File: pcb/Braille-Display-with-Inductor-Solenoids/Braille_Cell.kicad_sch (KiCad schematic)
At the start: 15 parts, among them U2 TPIC6595

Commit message: Remove symbol and footprint libraries
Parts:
- L1, L2, L3, L4, L5, L6: footprint 00-project-footprint-lib:Inductor_0805_2012Metric_SMD_Vertical_Square -> 00-project-footprints:Inductor_0805_2012Metric_SMD_Vertical_Square
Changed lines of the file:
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@@
 			)
 		)
-		(property "Footprint" "00-project-footprint-lib:Inductor_0805_2012Metric_SMD_Vertical_Square"
+		(property "Footprint" "00-project-footprints:Inductor_0805_2012Metric_SMD_Vertical_Square"
 			(at 107.95 66.04 0)
 			(effects
@@
 			)
 		)
-		(property "Footprint" "00-project-footprint-lib:Inductor_0805_2012Metric_SMD_Vertical_Square"
+		(property "Footprint" "00-project-footprints:Inductor_0805_2012Metric_SMD_Vertical_Square"
 			(at 107.95 52.07 0)
 			(effects
@@
 			)
 		)
-		(property "Footprint" "00-project-footprint-lib:Inductor_0805_2012Metric_SMD_Vertical_Square"
+		(property "Footprint" "00-project-footprints:Inductor_0805_2012Metric_SMD_Vertical_Square"
 			(at 121.92 66.04 0)
 			(effects
@@
 			)
 		)
-		(property "Footprint" "00-project-footprint-lib:Inductor_0805_2012Metric_SMD_Vertical_Square"
+		(property "Footprint" "00-project-footprints:Inductor_0805_2012Metric_SMD_Vertical_Square"
 			(at 107.95 38.1 0)
 			(effects
@@
 			)
 		)
-		(property "Footprint" "00-project-footprint-lib:Inductor_0805_2012Metric_SMD_Vertical_Square"
+		(property "Footprint" "00-project-footprints:Inductor_0805_2012Metric_SMD_Vertical_Square"
 			(at 121.92 38.1 0)
 			(effects
@@
 			)
 		)
-		(property "Footprint" "00-project-footprint-lib:Inductor_0805_2012Metric_SMD_Vertical_Square"
+		(property "Footprint" "00-project-footprints:Inductor_0805_2012Metric_SMD_Vertical_Square"
 			(at 121.92 52.07 0)
 			(effects

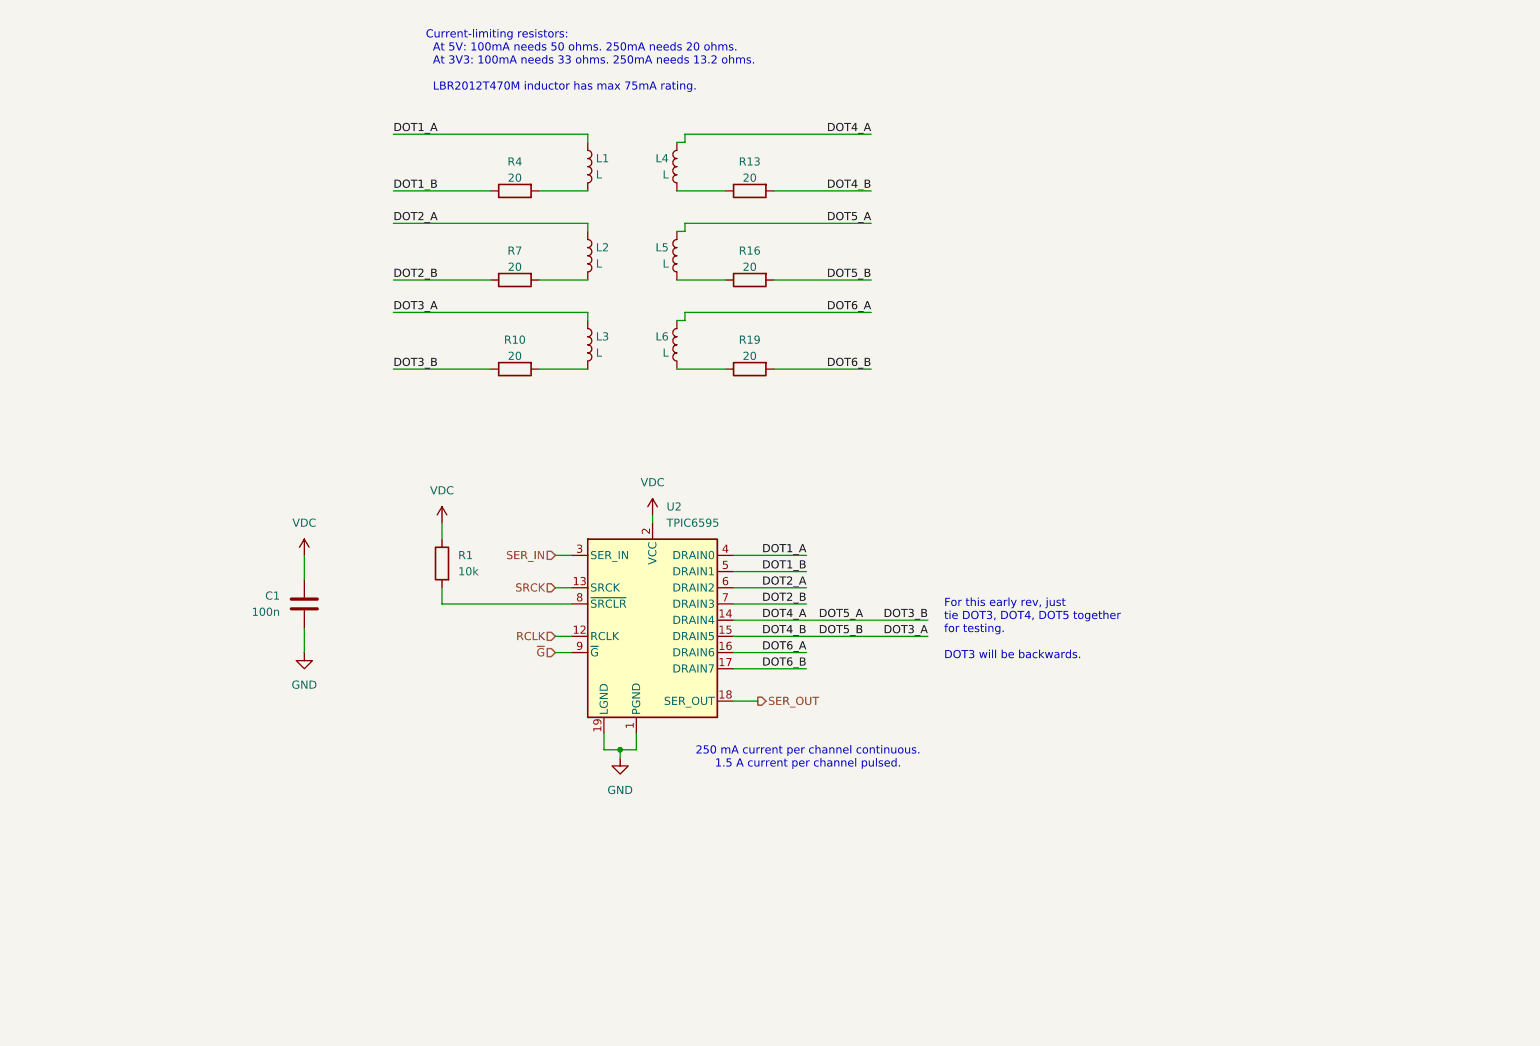
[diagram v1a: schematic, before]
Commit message: Add both inductors on same PCB, switch to new drivers
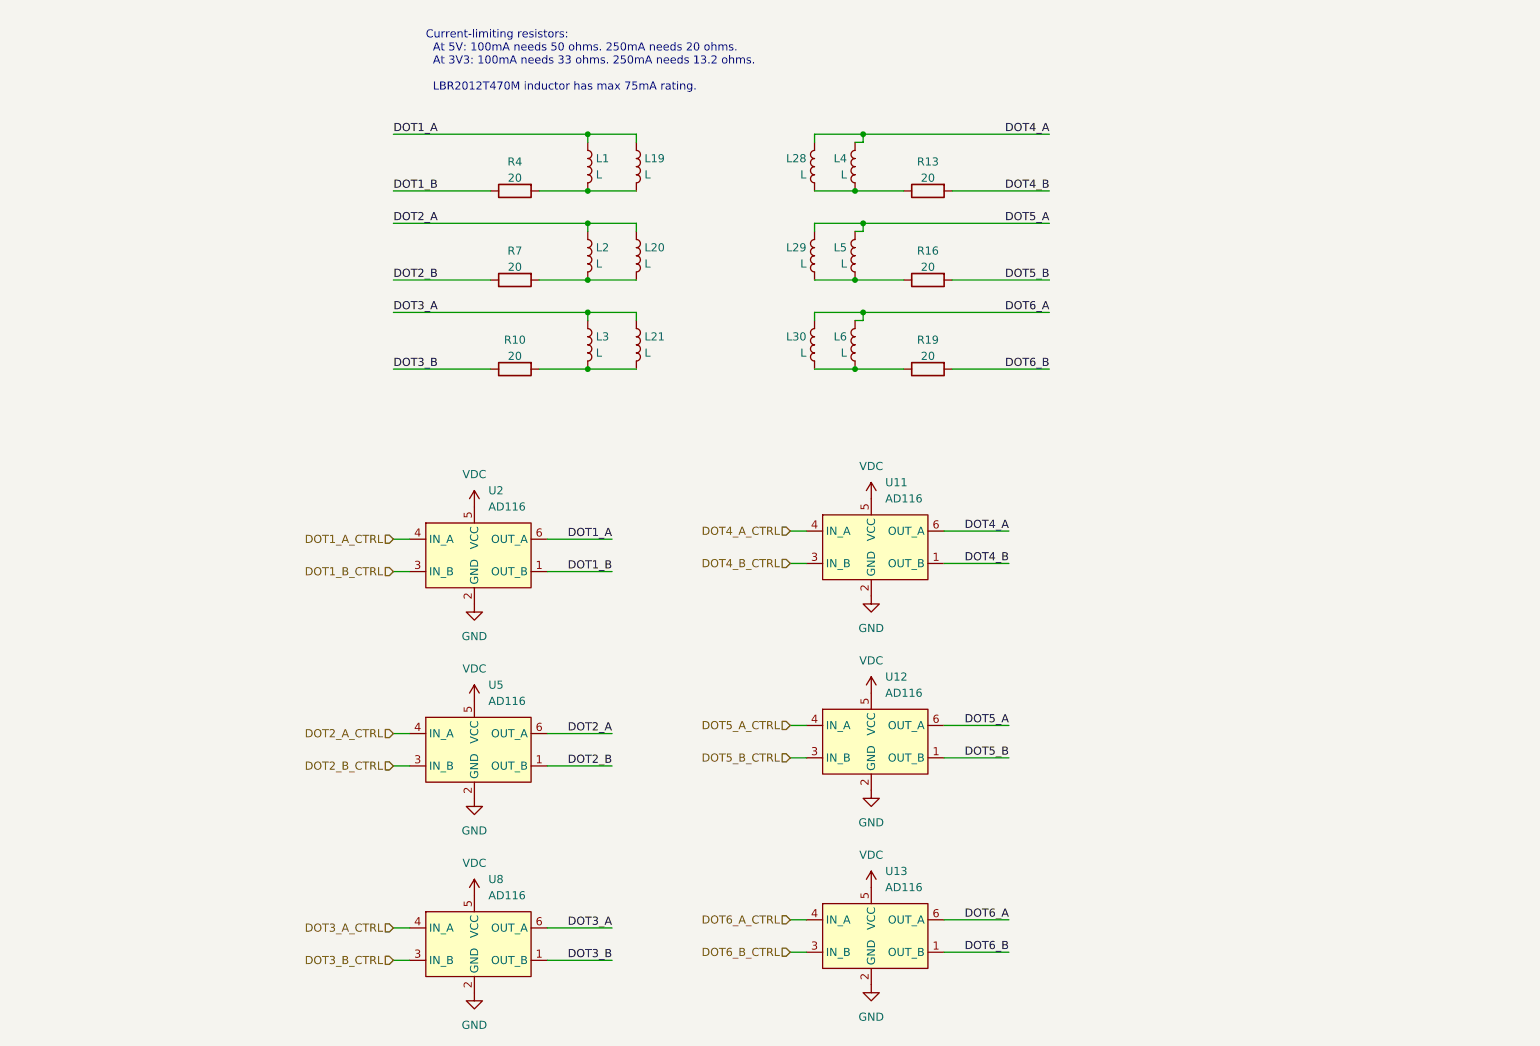
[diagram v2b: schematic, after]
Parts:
- removed C1: 100n, Capacitor_SMD:C_0603_1608Metric, symbol Device:C
- removed R1: 10k, Capacitor_SMD:C_0603_1608Metric_Pad1.08x0.95mm_HandSolder, symbol Device:R
- removed U2: TPIC6595, Package_SO:SOIC-20W_7.5x12.8mm_P1.27mm, symbol Interface_Expansion:TPIC6595
- added L19, L20, L21, L28, L29, L30: L, 00-project-footprints:Inductor_VLS201612CX, symbol Device:L
- added U11, U12, U13, U2, U5, U8: AD116, Package_TO_SOT_SMD:SOT-23-6, symbol 00-project-symbols:AD116_H_Bridge
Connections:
- net DOT1_A: now also L19.1, U2.6 (OUT_A)
- net DOT1_B: now also U2.1 (OUT_B)
- net DOT2_A: now also L20.1, U5.6 (OUT_A)
- net DOT2_B: now also U5.1 (OUT_B)
- net DOT3_A: now also L21.1, U8.6 (OUT_A); no longer R13.2, R16.2
- net DOT3_B: now also U8.1 (OUT_B); no longer L4.1, L5.1
- net DOT6_A: now also L30.1, U13.6 (OUT_A)
- net DOT6_B: now also U13.1 (OUT_B)
- net GND: now also U11.2 (GND), U12.2 (GND), U13.2 (GND), U2.2 (GND), U5.2 (GND), U8.2 (GND)
- net VDC: now also U11.5 (VCC), U12.5 (VCC), U13.5 (VCC), U2.5 (VCC), U5.5 (VCC), U8.5 (VCC)
- net at L3.2, R10.2: now also L21.2
- net at L2.2, R7.2: now also L20.2
- net at L6.2, R19.1: now also L30.2
- net at L1.2, R4.2: now also L19.2
- net at L4.2, R13.1: now also L28.2
- net at L5.2, R16.1: now also L29.2
- new net DOT1_A_CTRL: U2.4 (IN_A)
- new net DOT1_B_CTRL: U2.3 (IN_B)
- new net DOT2_A_CTRL: U5.4 (IN_A)
- new net DOT2_B_CTRL: U5.3 (IN_B)
- new net DOT3_A_CTRL: U8.4 (IN_A)
- new net DOT3_B_CTRL: U8.3 (IN_B)
- new net DOT4_A: L28.1, L4.1, U11.6 (OUT_A)
- new net DOT4_A_CTRL: U11.4 (IN_A)
- new net DOT4_B: R13.2, U11.1 (OUT_B)
- new net DOT4_B_CTRL: U11.3 (IN_B)
- new net DOT5_A: L29.1, L5.1, U12.6 (OUT_A)
- new net DOT5_A_CTRL: U12.4 (IN_A)
- new net DOT5_B: R16.2, U12.1 (OUT_B)
- new net DOT5_B_CTRL: U12.3 (IN_B)
- new net DOT6_A_CTRL: U13.4 (IN_A)
- new net DOT6_B_CTRL: U13.3 (IN_B)
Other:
- note removed: "250 mA current per channel continuous. 1.5 A current per channel pulsed."
- note removed: "For this early rev, just tie DOT3, DOT4, DOT5 together for testing. DOT3 will be backwards."
- moved on the sheet: L4, L5, L6, R13, R16, R19

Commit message: Add breakouts, shrink SMD vertical inductor cutouts, add braille cell (4x now)
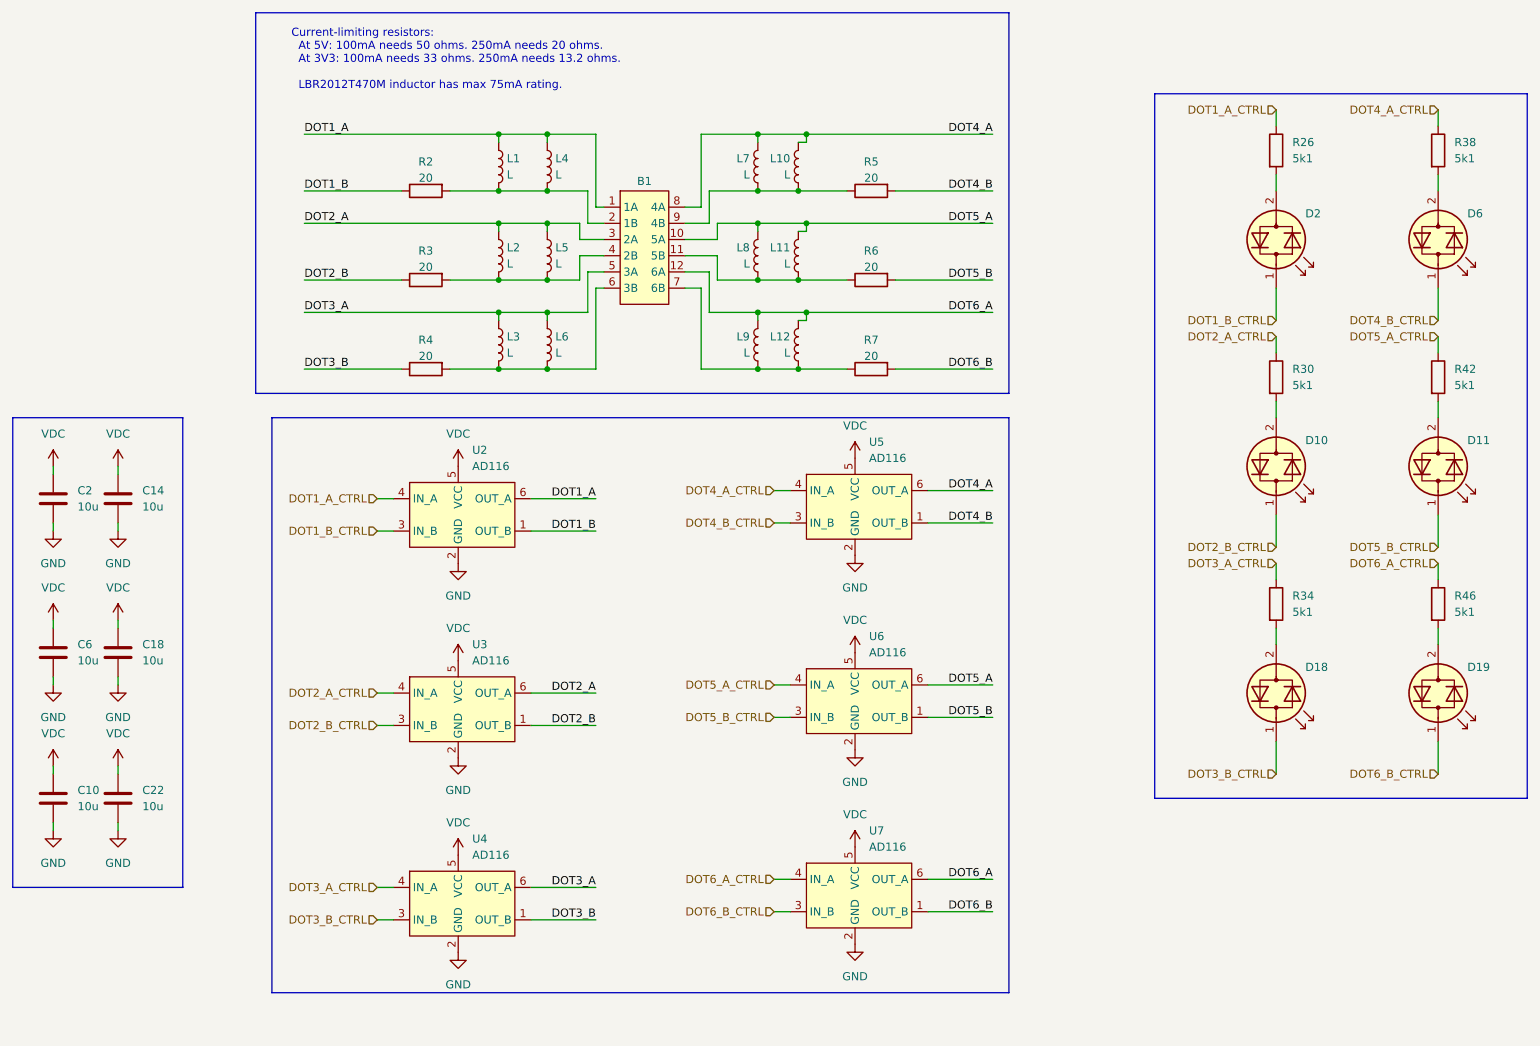
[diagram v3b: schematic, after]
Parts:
- added B1: ~, 00-project-footprints:Braille_Cell_Breakout, symbol 00-project-symbols:Braille_Cell_Breakout
- added C10, C14, C18, C2, C22, C6: 10u, Capacitor_SMD:C_1206_3216Metric_Pad1.33x1.80mm_HandSolder, symbol Device:C
- added D10, D11, D18, D19, D2, D6: LED_Dual_Bidirectional, 00-project-footprints:LED_0603_1608Metric_HandSolder_2x_Reverse, symbol Device:LED_Dual_Bidirectional
- added R26, R30, R34, R38, R42, R46: 5k1, Resistor_SMD:R_0603_1608Metric, symbol Device:R
- L1, L2, L3: footprint 00-project-footprints:Inductor_0805_2012Metric_SMD_Vertical_Square -> 00-project-footprints:Inductor_0805_2012Metric_SMD_Vertical_Square_Rev2_1.3mm
- L10: renamed from L4; footprint 00-project-footprints:Inductor_0805_2012Metric_SMD_Vertical_Square -> 00-project-footprints:Inductor_0805_2012Metric_SMD_Vertical_Square_Rev2_1.3mm
- L11: renamed from L5; footprint 00-project-footprints:Inductor_0805_2012Metric_SMD_Vertical_Square -> 00-project-footprints:Inductor_0805_2012Metric_SMD_Vertical_Square_Rev2_1.3mm
- L12: renamed from L6; footprint 00-project-footprints:Inductor_0805_2012Metric_SMD_Vertical_Square -> 00-project-footprints:Inductor_0805_2012Metric_SMD_Vertical_Square_Rev2_1.3mm
- renumbered L19 to L4, L20 to L5, L21 to L6, L28 to L7, L29 to L8, L30 to L9, R4 to R2, R7 to R3, R10 to R4, R13 to R5, R16 to R6, R19 to R7, U5 to U3, U8 to U4, U11 to U5, U12 to U6, U13 to U7
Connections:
- net DOT1_A: now also B1.1 (1A)
- net DOT1_A_CTRL: now also R26.1
- net DOT1_B_CTRL: now also D2.1 (KA)
- net DOT2_A: now also B1.3 (2A)
- net DOT2_A_CTRL: now also R30.1
- net DOT2_B_CTRL: now also D10.1 (KA)
- net DOT3_A: now also B1.5 (3A)
- net DOT3_A_CTRL: now also R34.1
- net DOT3_B_CTRL: now also D18.1 (KA)
- net DOT4_A: now also B1.8 (4A)
- net DOT4_A_CTRL: now also R38.1
- net DOT4_B_CTRL: now also D6.1 (KA)
- net DOT5_A: now also B1.10 (5A)
- net DOT5_A_CTRL: now also R42.1
- net DOT5_B_CTRL: now also D11.1 (KA)
- net DOT6_A: now also B1.12 (6A)
- net DOT6_A_CTRL: now also R46.1
- net DOT6_B_CTRL: now also D19.1 (KA)
- net GND: now also C10.2, C14.2, C18.2, C2.2, C22.2, C6.2
- net VDC: now also C10.1, C14.1, C18.1, C2.1, C22.1, C6.1
- net at L3.2, L6.2, R4.2: now also B1.6 (3B)
- net at L10.2, L7.2, R5.1: now also B1.9 (4B)
- net at L2.2, L5.2, R3.2: now also B1.4 (2B)
- net at L12.2, L9.2, R7.1: now also B1.7 (6B)
- net at L1.2, L4.2, R2.2: now also B1.2 (1B)
- net at L11.2, L8.2, R6.1: now also B1.11 (5B)
- new net: D11.2 (AK), R42.2
- new net: D18.2 (AK), R34.2
- new net: D10.2 (AK), R30.2
- new net: D2.2 (AK), R26.2
- new net: D19.2 (AK), R46.2
- new net: D6.2 (AK), R38.2
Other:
- moved on the sheet: L1, L10, L11, L12, L2, L3, L4, L5, L6, L7, L8, L9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

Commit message: Change page layout and reconnect components
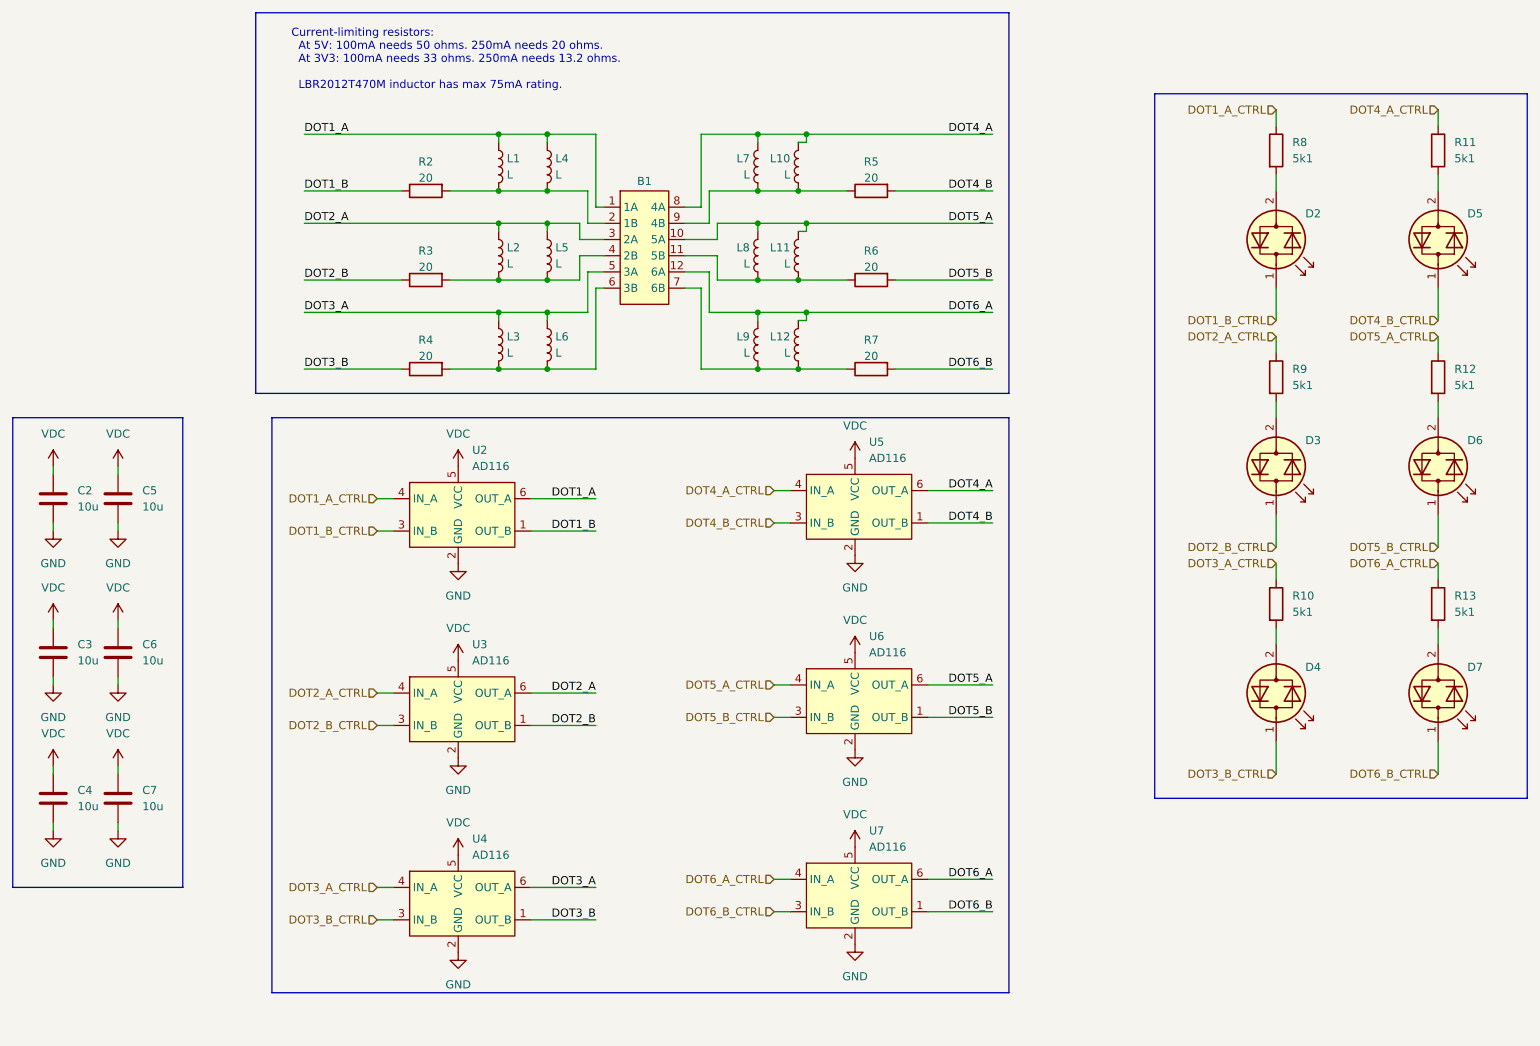
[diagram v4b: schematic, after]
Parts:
- renumbered C6 to C3, C10 to C4, C14 to C5, C18 to C6, C22 to C7, D10 to D3, D18 to D4, D6 to D5, D11 to D6, D19 to D7, R34 to R10, R38 to R11, R42 to R12, R46 to R13, R26 to R8, R30 to R9

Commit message: Layout debugging components
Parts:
- R10, R11, R12, R13, R8, R9: footprint Resistor_SMD:R_0603_1608Metric -> Resistor_SMD:R_0603_1608Metric_Pad0.98x0.95mm_HandSolder
- R2, R3, R4, R5, R6, R7: footprint Capacitor_SMD:C_0603_1608Metric_Pad1.08x0.95mm_HandSolder -> Resistor_SMD:R_0603_1608Metric_Pad0.98x0.95mm_HandSolder
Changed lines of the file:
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@@
 			)
 		)
-		(property "Footprint" "Resistor_SMD:R_0603_1608Metric"
+		(property "Footprint" "Resistor_SMD:R_0603_1608Metric_Pad0.98x0.95mm_HandSolder"
 			(at 239.522 71.12 90)
 			(effects
@@
 			)
 		)
-		(property "Footprint" "Resistor_SMD:R_0603_1608Metric"
+		(property "Footprint" "Resistor_SMD:R_0603_1608Metric_Pad0.98x0.95mm_HandSolder"
 			(at 214.122 106.68 90)
 			(effects
@@
 			)
 		)
-		(property "Footprint" "Capacitor_SMD:C_0603_1608Metric_Pad1.08x0.95mm_HandSolder"
+		(property "Footprint" "Resistor_SMD:R_0603_1608Metric_Pad0.98x0.95mm_HandSolder"
 			(at 152.4 68.072 90)
 			(effects
@@
 			)
 		)
-		(property "Footprint" "Resistor_SMD:R_0603_1608Metric"
+		(property "Footprint" "Resistor_SMD:R_0603_1608Metric_Pad0.98x0.95mm_HandSolder"
 			(at 214.122 71.12 90)
 			(effects
@@
 			)
 		)
-		(property "Footprint" "Capacitor_SMD:C_0603_1608Metric_Pad1.08x0.95mm_HandSolder"
+		(property "Footprint" "Resistor_SMD:R_0603_1608Metric_Pad0.98x0.95mm_HandSolder"
 			(at 82.55 40.132 90)
 			(effects
@@
 			)
 		)
-		(property "Footprint" "Capacitor_SMD:C_0603_1608Metric_Pad1.08x0.95mm_HandSolder"
+		(property "Footprint" "Resistor_SMD:R_0603_1608Metric_Pad0.98x0.95mm_HandSolder"
 			(at 82.55 54.102 90)
 			(effects
@@
 			)
 		)
-		(property "Footprint" "Resistor_SMD:R_0603_1608Metric"
+		(property "Footprint" "Resistor_SMD:R_0603_1608Metric_Pad0.98x0.95mm_HandSolder"
 			(at 214.122 35.56 90)
 			(effects
@@
 			)
 		)
-		(property "Footprint" "Capacitor_SMD:C_0603_1608Metric_Pad1.08x0.95mm_HandSolder"
+		(property "Footprint" "Resistor_SMD:R_0603_1608Metric_Pad0.98x0.95mm_HandSolder"
 			(at 152.4 54.102 90)
 			(effects
@@
 			)
 		)
-		(property "Footprint" "Resistor_SMD:R_0603_1608Metric"
+		(property "Footprint" "Resistor_SMD:R_0603_1608Metric_Pad0.98x0.95mm_HandSolder"
 			(at 239.522 106.68 90)
 			(effects
@@
 			)
 		)
-		(property "Footprint" "Capacitor_SMD:C_0603_1608Metric_Pad1.08x0.95mm_HandSolder"
+		(property "Footprint" "Resistor_SMD:R_0603_1608Metric_Pad0.98x0.95mm_HandSolder"
 			(at 152.4 40.132 90)
 			(effects
@@
 			)
 		)
-		(property "Footprint" "Resistor_SMD:R_0603_1608Metric"
+		(property "Footprint" "Resistor_SMD:R_0603_1608Metric_Pad0.98x0.95mm_HandSolder"
 			(at 239.522 35.56 90)
 			(effects
@@
 			)
 		)
-		(property "Footprint" "Capacitor_SMD:C_0603_1608Metric_Pad1.08x0.95mm_HandSolder"
+		(property "Footprint" "Resistor_SMD:R_0603_1608Metric_Pad0.98x0.95mm_HandSolder"
 			(at 82.55 68.072 90)
 			(effects
